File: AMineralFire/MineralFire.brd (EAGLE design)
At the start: 87 x 77 mm, 49 parts, among them IC1 LM358, Q1 20MHz, T1 200mA/40V, U1 328P, U3 7805

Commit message: added LED in switch
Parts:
- removed D4: Gate LED, SparkFun-LED:LED_3MM
- removed START: PB6149L-5, INSTRUO:PB6149L
- added BUT, BUT1: PB6149L-5, INSTRUO:PB6149L
- added PROGSW: (no value), INSTRUO:TOGGLE_ON_OFF_ON
- added R14: 1k, SparkFun-Resistors:AXIAL-0.3
- added R20, R21, R27: 100k, SparkFun-Resistors:AXIAL-0.3
- added R22: 10k, SparkFun-Resistors:AXIAL-0.3
- moved ISP1 17.8 mm to (80.0, 25.4)
- moved C7 8.98 mm to (73.7, 44.5)
- moved MODESW3 8.89 mm to (58.1, 10.2)
- moved C4 7.73 mm to (67.3, 44.5)
- moved C5 6.48 mm to (66.0, 52.1)
- moved D1 5.08 mm to (66.0, 57.1)
- moved R5 3.81 mm to (68.6, 27.9)
- moved R4 3.81 mm to (68.6, 31.8)
- moved R6 3.81 mm to (68.6, 24.1)
- moved R9 3.81 mm to (80.0, 31.8)
- moved C8 1.80 mm to (67.3, 38.1), turned to 180 degrees
- turned T1 to 0 degrees
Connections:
- new net N$16: BUT1.A, R27.P$2
- new net N$6: PROGSW.2, R14.P$1
- new net PR1: BUT1.1, BUT1.2, R22.P$1, R27.P$1, U1.11
- new net T7: PROGSW.1, R21.P$2, U1.12
- new net T8: PROGSW.3, R20.P$2, U1.13
- net +5V: now also R20.P$1, R21.P$1, R22.P$2
- net B_TRIG: now also BUT.1, BUT.2; no longer START.1, START.2
- net GND: now also BUT.3, BUT.4, BUT1.3, BUT1.4, BUT1.K, R14.P$2; no longer START.3, START.4
- net N$31: now also BUT.K; no longer D4.K
- net T1: now also U1.28; no longer U1.12
- net T2: now also U1.27; no longer U1.13
- net T3: now also U1.25; no longer U1.6
- net T4: now also U1.26; no longer U1.11
- net T5: no longer U1.2
- net T6: no longer U1.3
- net TRIGO: now also BUT.A; no longer D4.A
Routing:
- net PR1: track 0.00 -> 65.5 mm
- net N$31: track 8.47 -> 71.7 mm
- net T8: track 0.00 -> 41.1 mm
- net T7: track 0.00 -> 39.3 mm
- net GND: track 345.1 -> 381.7 mm
- net TRIGO: track 67.0 -> 93.9 mm
- net RST: track 72.9 -> 93.0 mm
- net T1: track 34.3 -> 54.3 mm
- net SCK: track 54.4 -> 39.7 mm
- net MOSI: track 51.0 -> 37.9 mm
- net MISO: track 49.6 -> 36.6 mm
- net +12V: track 113.0 -> 100.6 mm, vias 0 -> 1
- net +5V: track 255.0 -> 265.5 mm
- net T2: track 42.2 -> 50.5 mm
- net -12V: track 31.9 -> 23.8 mm
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- removed copper zone on layer 16, net GND
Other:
- board text added: "Workshop of Telescopes"

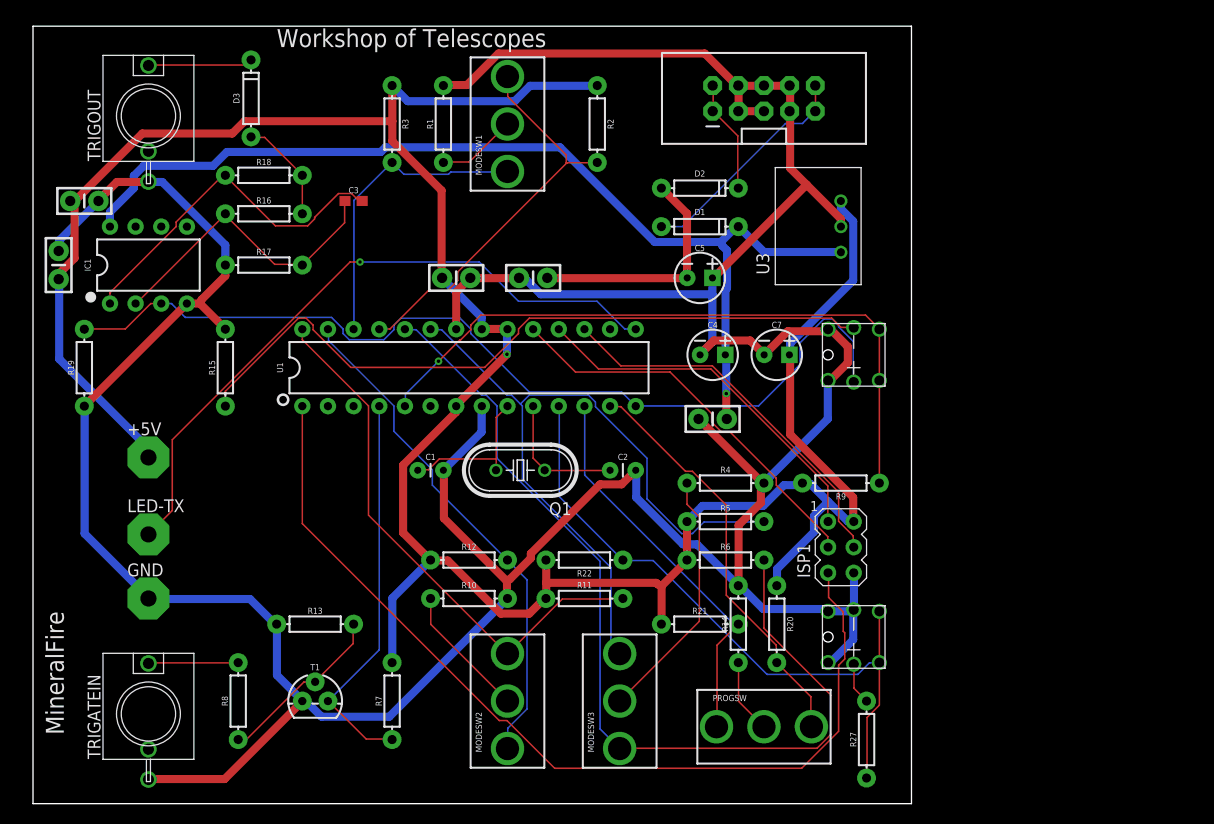
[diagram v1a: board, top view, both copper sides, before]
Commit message: Added AND gate on trigger
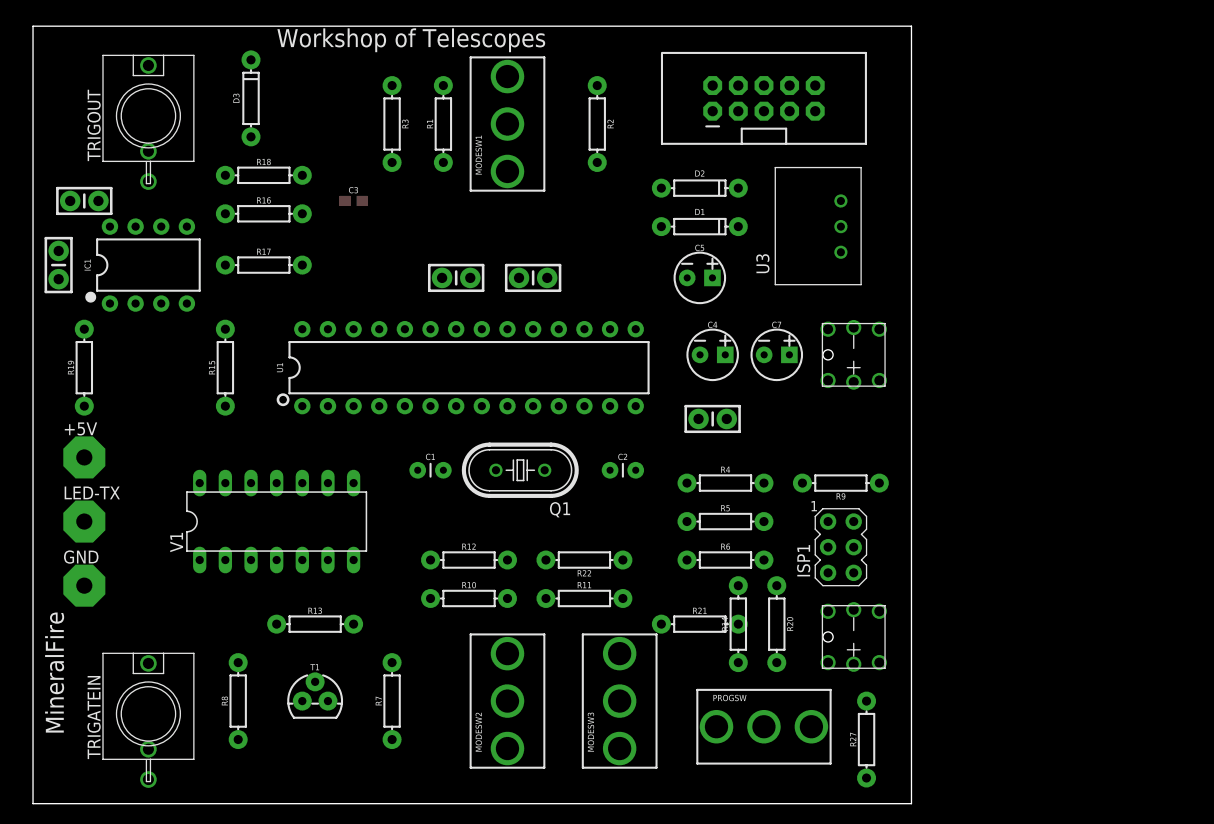
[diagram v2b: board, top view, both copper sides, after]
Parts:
- added V1: 7408N, 74ttl-din:DIL14
- moved GND 6.48 mm to (5.08, 21.6)
- moved LED-TX 6.48 mm to (5.08, 27.9)
- moved +5V 6.35 mm to (5.08, 34.3)
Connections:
- new net LBUTTON: BUT1.1, BUT1.2, R22.P$1, R27.P$1, V1.2
- new net LTRIG: R7.P$1, T1.3, V1.1
- net +5V: now also V1.14
- net GND: now also V1.7
- net PR1: no longer BUT1.1, BUT1.2, R22.P$1, R27.P$1
- net TRIG: now also V1.3; no longer R7.P$1, T1.3
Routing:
- net GND: track 381.7 -> 0.00 mm
- net +5V: track 265.5 -> 0.00 mm, vias 1 -> 0
- net +12V: track 100.6 -> 0.00 mm, vias 1 -> 0
- net TRIGO: track 93.9 -> 0.00 mm
- net RST: track 93.0 -> 0.00 mm
- net T6: track 92.7 -> 0.00 mm
- net T5: track 74.1 -> 0.00 mm
- net N$31: track 71.7 -> 0.00 mm
- net B_TRIG: track 67.5 -> 0.00 mm, vias 1 -> 0
- net N$5: track 66.3 -> 0.00 mm, vias 1 -> 0
- net PR1: track 65.5 -> 0.00 mm
- net T1: track 54.3 -> 0.00 mm
- net T2: track 50.5 -> 0.00 mm
- net T8: track 41.1 -> 0.00 mm
- net T3: track 39.9 -> 0.00 mm
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
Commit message: LED in count switch
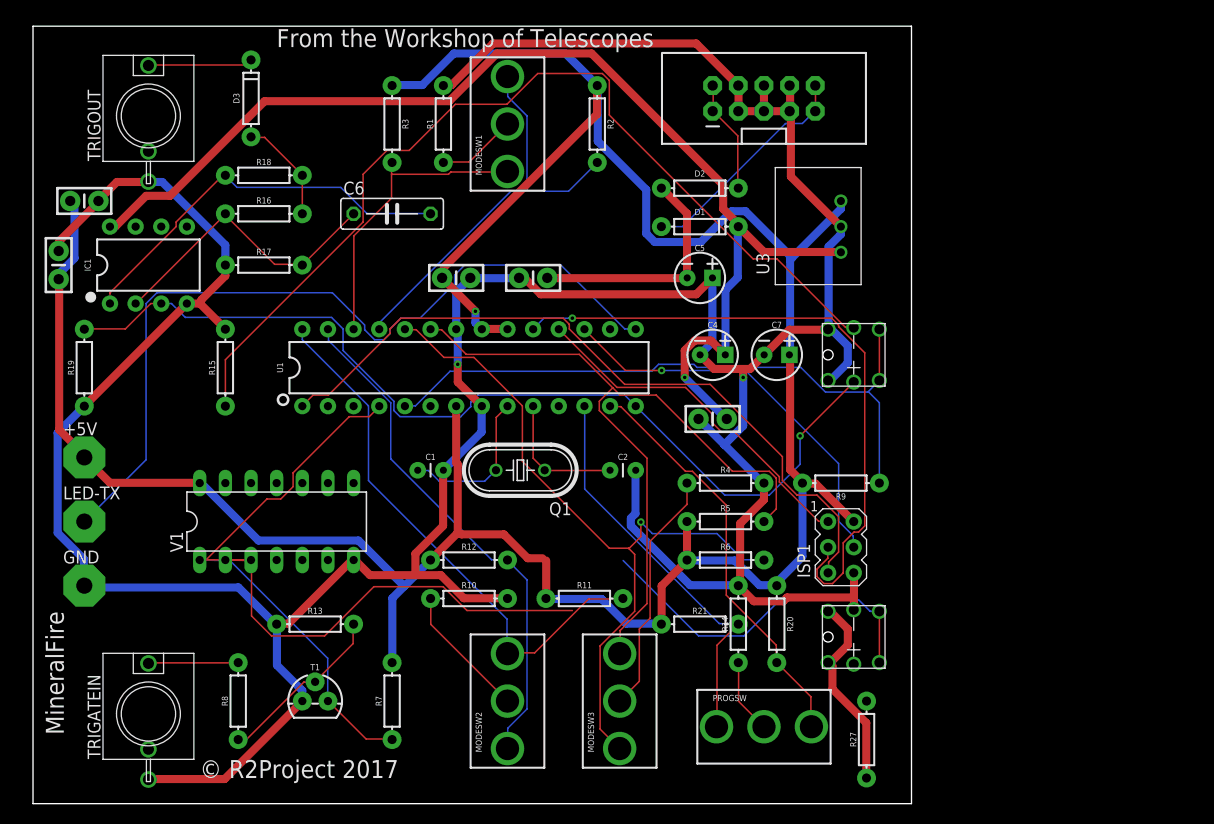
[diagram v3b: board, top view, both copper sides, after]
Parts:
- removed C3: 100pF, SparkFun-Capacitors:0603
- removed R22: 10k, SparkFun-Resistors:AXIAL-0.3
- added C6: 100pf, rcl:C075-032X103
- R27: value 100k -> 150
- V1: value 7408N -> 7432N
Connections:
- removed net N$16: BUT1.A, R27.P$2
- new net N$11: BUT1.3, BUT1.4, BUT1.A
- net +5V: now also R27.P$1; no longer R22.P$2
- net GND: no longer BUT1.3, BUT1.4
- net LBUTTON: now also R27.P$2; no longer R22.P$1, R27.P$1
- net N$32: now also C6.1; no longer C3.1
- net N$33: now also C6.2; no longer C3.2
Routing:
- net GND: track 0.00 -> 365.5 mm, vias 0 -> 2
- net +5V: track 0.00 -> 279.9 mm, vias 0 -> 1
- net +12V: track 0.00 -> 116.0 mm, vias 0 -> 1
- net TRIGO: track 0.00 -> 95.2 mm, vias 0 -> 1
- net N$31: track 0.00 -> 93.8 mm
- net N$5: track 0.00 -> 81.7 mm
- net LBUTTON: track 0.00 -> 79.2 mm
- net T5: track 0.00 -> 75.1 mm
- net T6: track 0.00 -> 73.5 mm, vias 0 -> 1
- net RST: track 0.00 -> 72.8 mm
- net B_TRIG: track 0.00 -> 64.9 mm
- net SCK: track 0.00 -> 64.5 mm, vias 0 -> 1
- net T1: track 0.00 -> 54.3 mm
- net T2: track 0.00 -> 51.4 mm
- net T8: track 0.00 -> 41.1 mm
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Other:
- board text added: "From the Workshop of Telescopes"
- board text added: "© R2Project 2017"
- board text removed: "Workshop of Telescopes"

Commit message: Board too big
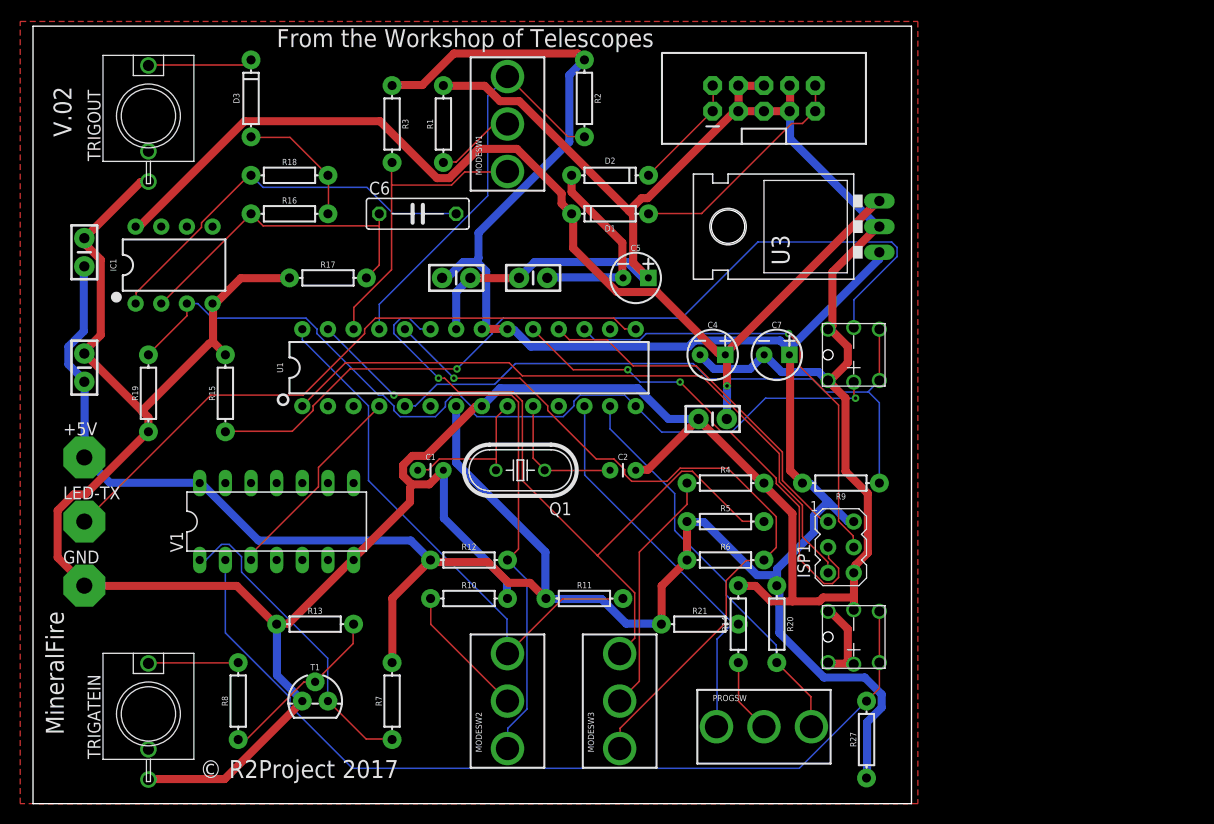
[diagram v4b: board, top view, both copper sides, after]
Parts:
- U3: device SparkFun-IC-Power:DC-DC_CONVERTER_78XX -> SparkFun-IC-Power:TO-220-ALT
- moved C12 10.5 mm to (5.08, 43.2)
- moved D1 8.98 mm to (57.1, 58.4), turned to 180 degrees
- moved D2 8.98 mm to (57.1, 62.2)
- moved R19 6.84 mm to (11.4, 40.6)
- moved R17 6.48 mm to (29.2, 52.1)
- moved C5 6.35 mm to (59.7, 52.1)
- moved C11 5.08 mm to (5.08, 54.6), turned to 90 degrees
- moved R2 2.84 mm to (54.6, 69.8)
- moved IC1 2.54 mm to (14.0, 53.3)
- moved C6 2.54 mm to (38.1, 58.4)
- moved R15 2.54 mm to (19.1, 40.6)
- moved R16 2.54 mm to (25.4, 58.4)
- moved R18 2.54 mm to (25.4, 62.2)
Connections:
- net +12V: now also U3.OUT; no longer U3.VIN
- net +5V: now also U3.IN; no longer U3.VOUT
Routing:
- net GND: track 365.5 -> 399.7 mm, vias 2 -> 0
- net +5V: track 279.9 -> 300.1 mm, vias 1 -> 0
- net N$5: track 81.7 -> 63.7 mm
- net SCK: track 64.5 -> 48.2 mm, vias 1 -> 2
- net N$11: track 19.9 -> 9.06 mm
- net +12V: track 116.0 -> 105.3 mm
- net LBUTTON: track 79.2 -> 88.9 mm
- net TRIG: track 29.9 -> 20.5 mm
- net TRIGO: track 95.2 -> 86.1 mm
- net N$31: track 93.8 -> 84.8 mm, vias 0 -> 1
- net T2: track 51.4 -> 58.2 mm, vias 0 -> 1
- net RST: track 72.8 -> 66.6 mm
- net MOSI: track 39.6 -> 44.7 mm
- net -12V: track 23.8 -> 19.8 mm
- net N$32: track 29.6 -> 32.7 mm
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- added copper zone on layer 1, net GND
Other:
- board text added: "V.02"

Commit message: Shrunk board by 5mm
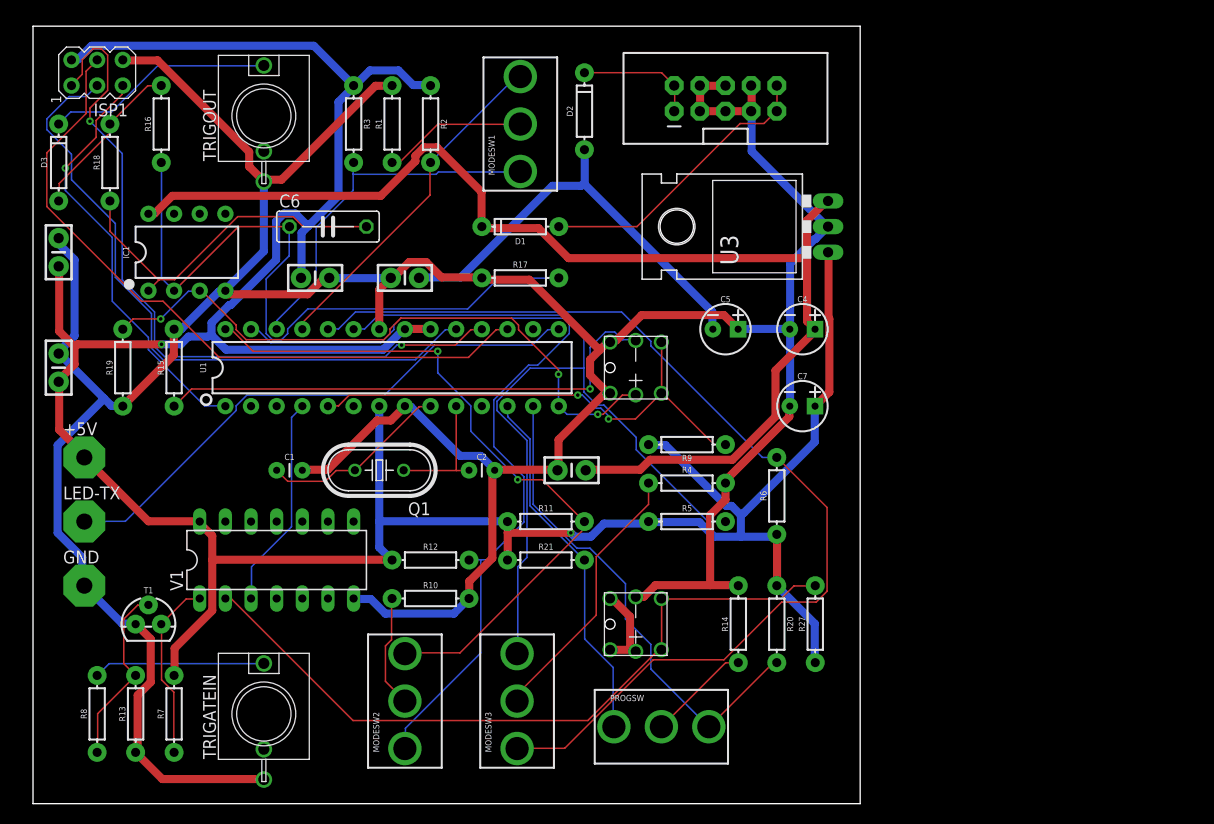
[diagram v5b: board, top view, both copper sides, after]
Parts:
- moved ISP1 87.4 mm to (6.35, 72.4), turned to 90 degrees
- moved BUT 21.6 mm to (59.7, 43.2)
- moved BUT1 21.6 mm to (59.7, 17.8)
- moved R7 21.6 mm to (14.0, 8.89)
- moved D3 20.1 mm to (2.54, 63.5)
- moved R13 19.9 mm to (10.2, 8.89), turned to 90 degrees
- moved R17 19.0 mm to (48.3, 52.1)
- moved T1 18.2 mm to (11.4, 17.8)
- moved R18 17.8 mm to (7.62, 63.5), turned to 90 degrees
- moved R21 16.5 mm to (50.8, 24.1)
- moved R9 15.7 mm to (64.8, 35.6)
- moved R16 15.5 mm to (12.7, 67.3), turned to 90 degrees
- moved R2 15.5 mm to (39.4, 67.3)
- moved C8 14.9 mm to (53.3, 33.0)
- moved R8 14.0 mm to (6.35, 8.89)
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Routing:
- net N$32: track 32.7 -> 70.9 mm
- net GND: track 399.7 -> 362.2 mm
- net MISO: track 36.2 -> 72.4 mm, vias 0 -> 2
- net N$31: track 84.8 -> 51.5 mm
- net T2: track 58.2 -> 86.9 mm, vias 1 -> 0
- net T6: track 76.5 -> 103.9 mm, vias 1 -> 0
- net MOSI: track 44.7 -> 69.5 mm, vias 1 -> 0
- net RST: track 66.6 -> 41.9 mm, vias 0 -> 1
- net -12V: track 19.8 -> 43.3 mm
- net TRIGO: track 86.1 -> 62.9 mm, vias 1 -> 3
- net SCK: track 48.2 -> 65.3 mm, vias 2 -> 0
- net LBUTTON: track 88.9 -> 72.0 mm
- net B_TRIG: track 65.0 -> 49.3 mm, vias 0 -> 2
- net T1: track 54.2 -> 69.9 mm, vias 0 -> 2
- net +12V: track 105.3 -> 120.0 mm, vias 1 -> 0
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- removed copper zone on layer 1, net GND
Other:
- board size 87 x 77 mm -> 81.9 x 77 mm
- board text added: "@R2Project. Designed by Andy C Grateful to GMSN! for all their help!"
- board text added: "Mineral Fire"
- board text removed: "MineralFire"
- board text removed: "V.02"
- board text removed: "© R2Project 2017"

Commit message: Larger Board
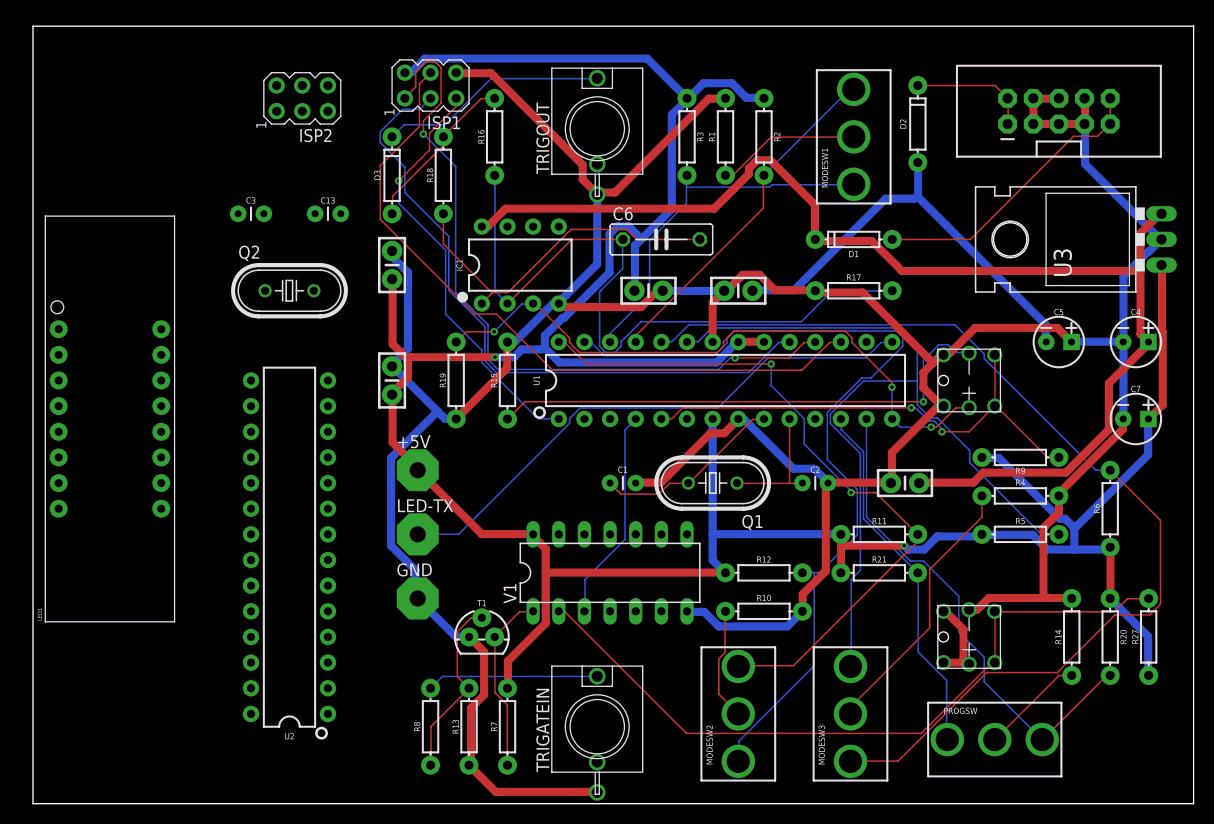
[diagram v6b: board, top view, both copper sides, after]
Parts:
- added C13, C3: 22pF, SparkFun-Capacitors:CAP-PTH-2.54
- added ISP2: AVRISP-6, adafruit:AVRISP
- added LED1: YSD-439AB4B-35, SparkFun-LED:7-SEGMENT-4DIGIT-YOUNGSUN
- added Q2: 20MHz, adafruit:HC49U70
- added U2: 328P, SparkFun-IC-Microcontroller:DIP28
- moved R14 33.0 mm to (102.9, 16.5)
- moved R20 33.0 mm to (106.7, 16.5)
- moved R4 33.0 mm to (97.8, 30.5)
- moved R5 33.0 mm to (97.8, 26.7)
- moved R6 33.0 mm to (106.7, 29.2)
- moved R9 33.0 mm to (97.8, 34.3)
- moved +5V 33.0 mm to (38.1, 33.0)
- moved C1 33.0 mm to (58.4, 31.8)
- moved C11 33.0 mm to (35.6, 53.3)
- moved C12 33.0 mm to (35.6, 41.9)
- moved D1 33.0 mm to (81.3, 55.9)
- moved D3 33.0 mm to (35.6, 62.2)
- moved GND 33.0 mm to (38.1, 20.3)
- moved LED-TX 33.0 mm to (38.1, 26.7)
- moved MODESW1 33.0 mm to (81.3, 66.0)
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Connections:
- new net N$7: C3.1, Q2.2, U2.9
- new net N$8: C13.1, Q2.1, U2.10
- net +5V: now also ISP2.2, U2.20, U2.21, U2.7
- net GND: now also C13.2, C3.2, ISP2.6, U2.22, U2.8
- net MISO: now also ISP2.1
- net MOSI: now also ISP2.4
- net RST: now also ISP2.5, U2.1
- net SCK: now also ISP2.3
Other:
- board size 81.9 x 77 mm -> 114.9 x 77 mm
